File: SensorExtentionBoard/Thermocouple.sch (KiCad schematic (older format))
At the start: 13 parts

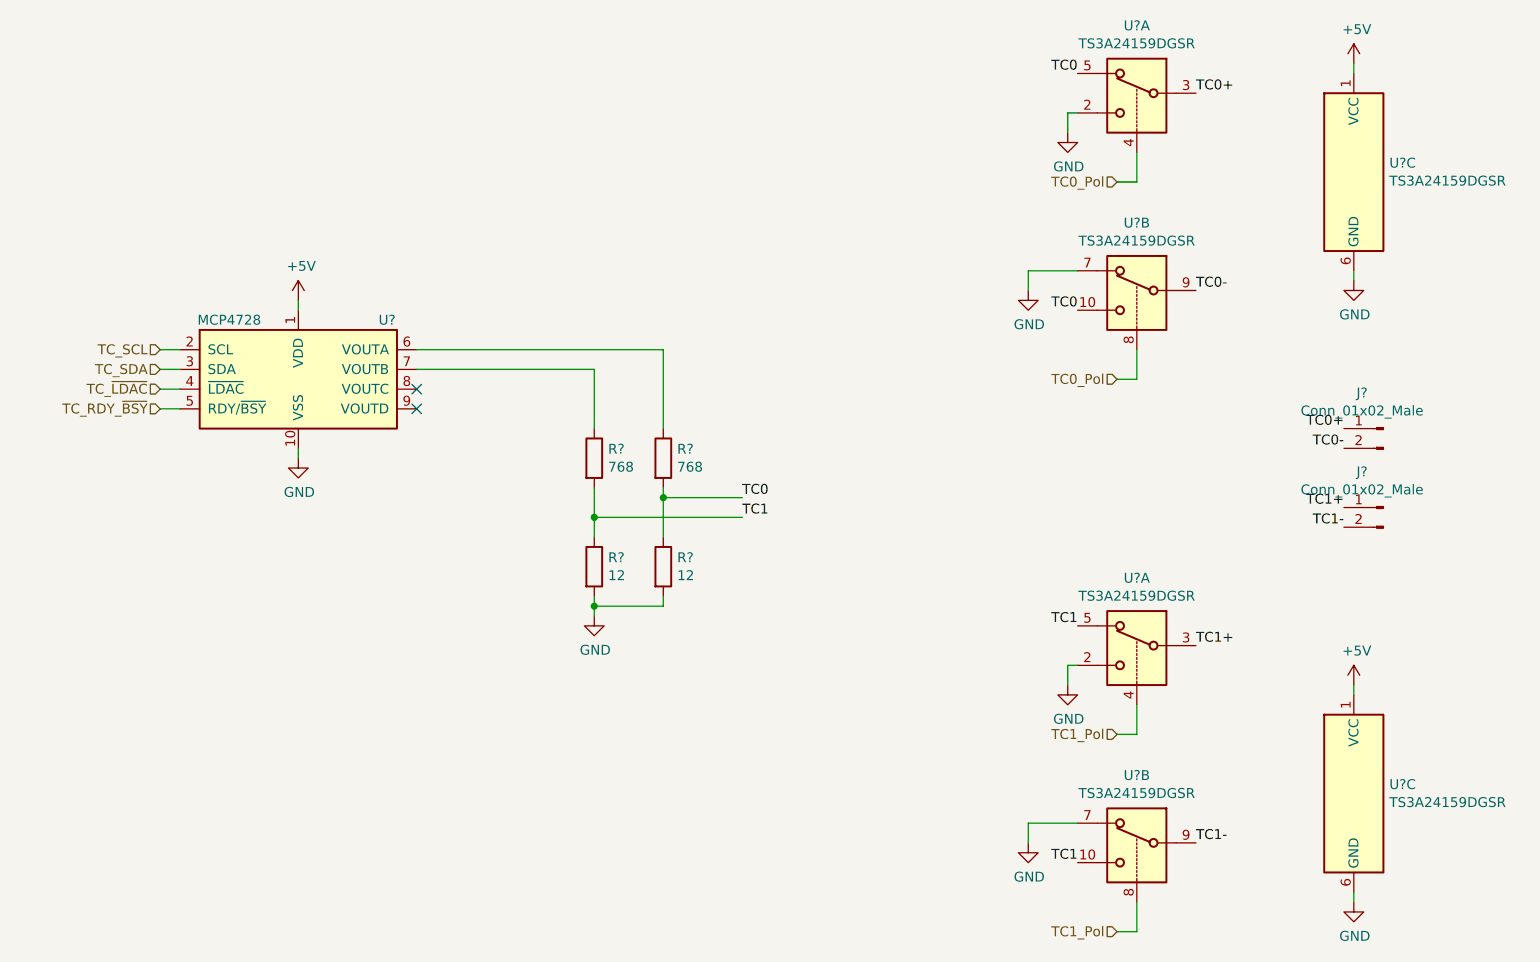
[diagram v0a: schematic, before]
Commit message: Added top level page and made various fixes in other pages of SEB test rig board
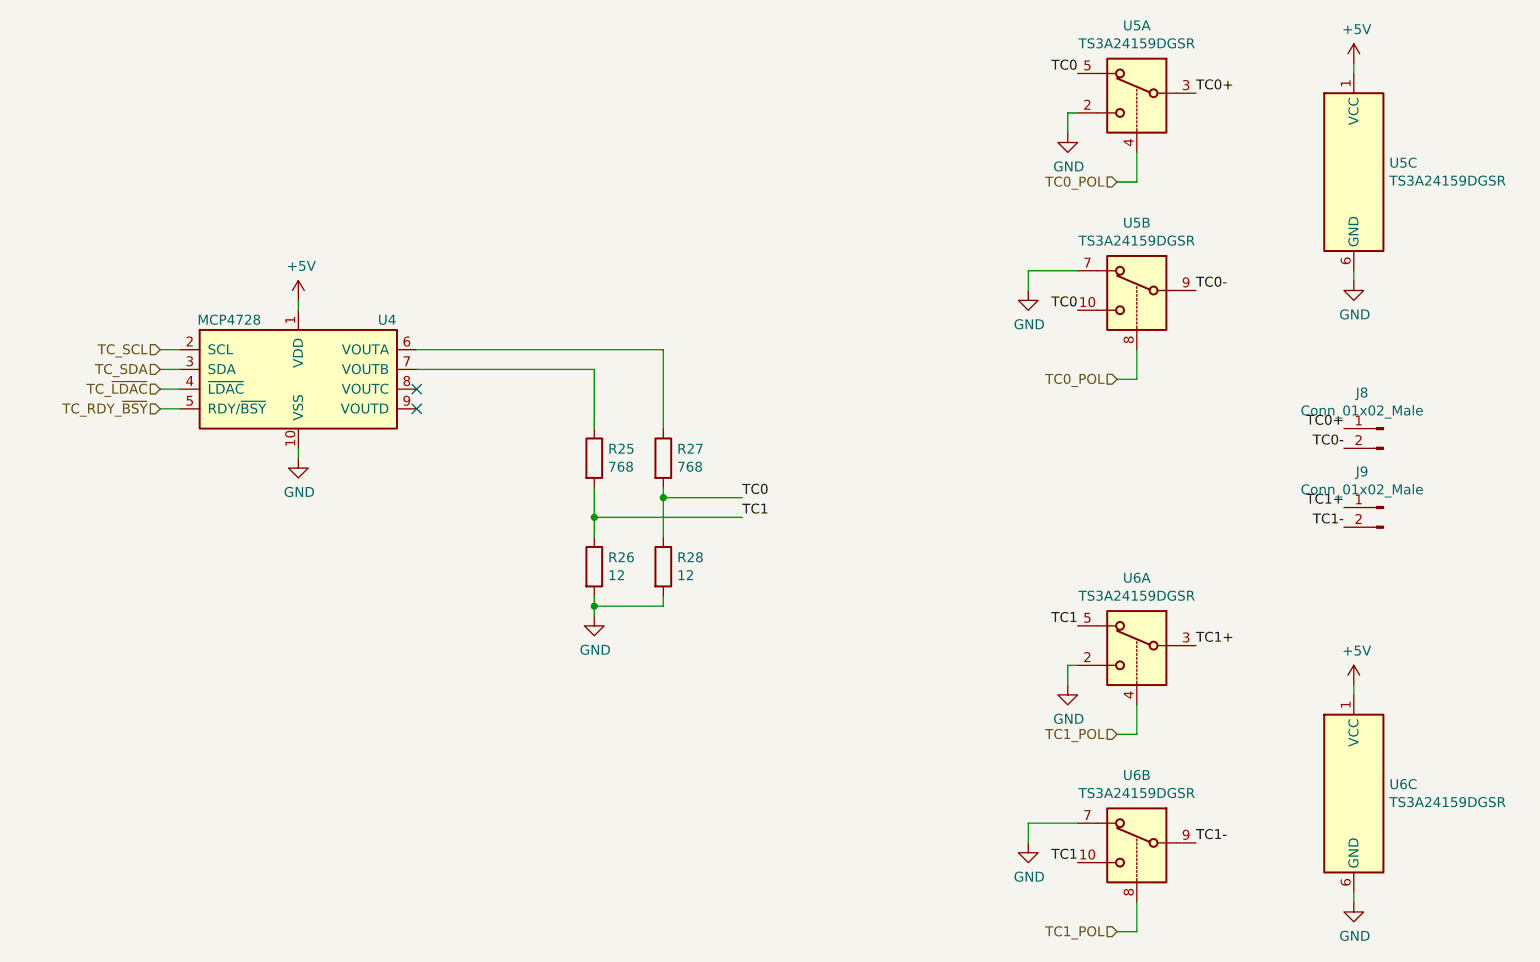
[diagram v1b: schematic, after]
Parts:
- R25, R26, R27, R28: renamed from R?; footprint (none) -> Resistor_SMD:R_1206_3216Metric_Pad1.42x1.75mm_HandSolder
- gave numbers to parts that had none: 5
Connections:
- net TC0_Pol renamed TC0_POL
- net TC1_Pol renamed TC1_POL
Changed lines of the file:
@@
 $EndDescr
 $Comp
-L Analog_DAC:MCP4728 U?
+L Analog_DAC:MCP4728 U4
 U 1 1 5E2FD865
 P 4000 2350
-F 0 "U?" H 4450 2600 50  0000 C CNN
+F 0 "U4" H 4450 2600 50  0000 C CNN
 F 1 "MCP4728" H 3650 2600 50  0000 C CNN
 F 2 "Package_SO:MSOP-10_3x3mm_P0.5mm" H 4000 1750 50  0001 C CNN
@@
 $EndComp
 $Comp
-L power:GND #PWR?
+L power:GND #PWR022
 U 1 1 5E2FE6B0
 P 4000 2800
-F 0 "#PWR?" H 4000 2550 50  0001 C CNN
+F 0 "#PWR022" H 4000 2550 50  0001 C CNN
 F 1 "GND" H 4005 2627 50  0000 C CNN
 F 2 "" H 4000 2800 50  0001 C CNN
@@
 	4000 2800 4000 2750
 $Comp
-L power:+5V #PWR?
+L power:+5V #PWR021
 U 1 1 5E2FE9D8
 P 4000 2000
-F 0 "#PWR?" H 4000 1850 50  0001 C CNN
+F 0 "#PWR021" H 4000 1850 50  0001 C CNN
 F 1 "+5V" H 4015 2173 50  0000 C CNN
 F 2 "" H 4000 2000 50  0001 C CNN
@@
 	3300 2450 3400 2450
 $Comp
-L Device:R R?
+L Device:R R27
 U 1 1 5E3006EF
 P 5850 2800
-F 0 "R?" H 5920 2846 50  0000 L CNN
+F 0 "R27" H 5920 2846 50  0000 L CNN
 F 1 "768" H 5920 2755 50  0000 L CNN
-F 2 "" V 5780 2800 50  0001 C CNN
+F 2 "Resistor_SMD:R_1206_3216Metric_Pad1.42x1.75mm_HandSolder" V 5780 2800 50  0001 C CNN
 F 3 "~" H 5850 2800 50  0001 C CNN
 	1    5850 2800
@@
 $EndComp
 $Comp
-L Device:R R?
+L Device:R R28
 U 1 1 5E300948
 P 5850 3350
-F 0 "R?" H 5920 3396 50  0000 L CNN
+F 0 "R28" H 5920 3396 50  0000 L CNN
 F 1 "12" H 5920 3305 50  0000 L CNN
-F 2 "" V 5780 3350 50  0001 C CNN
+F 2 "Resistor_SMD:R_1206_3216Metric_Pad1.42x1.75mm_HandSolder" V 5780 3350 50  0001 C CNN
 F 3 "~" H 5850 3350 50  0001 C CNN
 	1    5850 3350
@@
 $EndComp
 $Comp
-L Device:R R?
+L Device:R R25
 U 1 1 5E3082B4
 P 5500 2800
-F 0 "R?" H 5570 2846 50  0000 L CNN
+F 0 "R25" H 5570 2846 50  0000 L CNN
 F 1 "768" H 5570 2755 50  0000 L CNN
-F 2 "" V 5430 2800 50  0001 C CNN
+F 2 "Resistor_SMD:R_1206_3216Metric_Pad1.42x1.75mm_HandSolder" V 5430 2800 50  0001 C CNN
 F 3 "~" H 5500 2800 50  0001 C CNN
 	1    5500 2800
@@
 $EndComp
 $Comp
-L Device:R R?
+L Device:R R26
 U 1 1 5E3082BA
 P 5500 3350
-F 0 "R?" H 5570 3396 50  0000 L CNN
+F 0 "R26" H 5570 3396 50  0000 L CNN
 F 1 "12" H 5570 3305 50  0000 L CNN
-F 2 "" V 5430 3350 50  0001 C CNN
+F 2 "Resistor_SMD:R_1206_3216Metric_Pad1.42x1.75mm_HandSolder" V 5430 3350 50  0001 C CNN
 F 3 "~" H 5500 3350 50  0001 C CNN
 	1    5500 3350
@@
 	5500 3100 5500 3200
 $Comp
-L power:GND #PWR?
+L power:GND #PWR023
 U 1 1 5E3159B6
 P 5500 3600
-F 0 "#PWR?" H 5500 3350 50  0001 C CNN
+F 0 "#PWR023" H 5500 3350 50  0001 C CNN
 F 1 "GND" H 5505 3427 50  0000 C CNN
 F 2 "" H 5500 3600 50  0001 C CNN
@@
 NoConn ~ 4600 2450
 $Comp
-L Analog_Switch:TS3A24159DGSR U?
+L Analog_Switch:TS3A24159DGSR U5
 U 3 1 5E318CFB
 P 9350 1350
-F 0 "U?" H 9530 1396 50  0000 L CNN
+F 0 "U5" H 9530 1396 50  0000 L CNN
 F 1 "TS3A24159DGSR" H 9530 1305 50  0000 L CNN
 F 2 "Package_SO:TSSOP-10_3x3mm_P0.5mm" H 9350 1000 50  0001 C CNN
@@
 $EndComp
 $Comp
-L power:+5V #PWR?
+L power:+5V #PWR028
 U 1 1 5E33134D
 P 9350 800
-F 0 "#PWR?" H 9350 650 50  0001 C CNN
+F 0 "#PWR028" H 9350 650 50  0001 C CNN
 F 1 "+5V" H 9365 973 50  0000 C CNN
 F 2 "" H 9350 800 50  0001 C CNN
@@
 	9350 800  9350 850
 $Comp
-L power:GND #PWR?
+L power:GND #PWR029
 U 1 1 5E332A5C
 P 9350 1900
-F 0 "#PWR?" H 9350 1650 50  0001 C CNN
+F 0 "#PWR029" H 9350 1650 50  0001 C CNN
 F 1 "GND" H 9355 1727 50  0000 C CNN
 F 2 "" H 9350 1900 50  0001 C CNN
@@
 	8150 2400 8250 2400
 Text HLabel 8150 2400 0    50   Input ~ 0
-TC0_Pol
+TC0_POL
 Wire Wire Line
 	8250 1400 8250 1250
@@
 	8150 1400 8250 1400
 Text HLabel 8150 1400 0    50   Input ~ 0
-TC0_Pol
+TC0_POL
 Wire Wire Line
 	7900 1050 7950 1050
@@
 TC0
 $Comp
-L power:GND #PWR?
+L power:GND #PWR024
 U 1 1 5E324555
 P 7700 1950
-F 0 "#PWR?" H 7700 1700 50  0001 C CNN
+F 0 "#PWR024" H 7700 1700 50  0001 C CNN
 F 1 "GND" H 7705 1777 50  0000 C CNN
 F 2 "" H 7700 1950 50  0001 C CNN
@@
 $EndComp
 $Comp
-L power:GND #PWR?
+L power:GND #PWR026
 U 1 1 5E324066
 P 7900 1150
-F 0 "#PWR?" H 7900 900 50  0001 C CNN
+F 0 "#PWR026" H 7900 900 50  0001 C CNN
 F 1 "GND" H 7905 977 50  0000 C CNN
 F 2 "" H 7900 1150 50  0001 C CNN
@@
 TC0+
 $Comp
-L Analog_Switch:TS3A24159DGSR U?
+L Analog_Switch:TS3A24159DGSR U5
 U 2 1 5E317F40
 P 8250 1850
-F 0 "U?" H 8250 2092 50  0000 C CNN
+F 0 "U5" H 8250 2092 50  0000 C CNN
 F 1 "TS3A24159DGSR" H 8250 2001 50  0000 C CNN
 F 2 "Package_SO:TSSOP-10_3x3mm_P0.5mm" H 8250 1500 50  0001 C CNN
@@
 $EndComp
 $Comp
-L Analog_Switch:TS3A24159DGSR U?
+L Analog_Switch:TS3A24159DGSR U5
 U 1 1 5E31745F
 P 8250 850
-F 0 "U?" H 8250 1092 50  0000 C CNN
+F 0 "U5" H 8250 1092 50  0000 C CNN
 F 1 "TS3A24159DGSR" H 8250 1001 50  0000 C CNN
 F 2 "Package_SO:TSSOP-10_3x3mm_P0.5mm" H 8250 500 50  0001 C CNN
@@
 $EndComp
 $Comp
-L Analog_Switch:TS3A24159DGSR U?
+L Analog_Switch:TS3A24159DGSR U6
 U 3 1 5E35C1F5
 P 9350 4500
-F 0 "U?" H 9530 4546 50  0000 L CNN
+F 0 "U6" H 9530 4546 50  0000 L CNN
 F 1 "TS3A24159DGSR" H 9530 4455 50  0000 L CNN
 F 2 "Package_SO:TSSOP-10_3x3mm_P0.5mm" H 9350 4150 50  0001 C CNN
@@
 $EndComp
 $Comp
-L power:+5V #PWR?
+L power:+5V #PWR030
 U 1 1 5E35C1FB
 P 9350 3950
-F 0 "#PWR?" H 9350 3800 50  0001 C CNN
+F 0 "#PWR030" H 9350 3800 50  0001 C CNN
 F 1 "+5V" H 9365 4123 50  0000 C CNN
 F 2 "" H 9350 3950 50  0001 C CNN
@@
 	9350 3950 9350 4000
 $Comp
-L power:GND #PWR?
+L power:GND #PWR031
 U 1 1 5E35C202
 P 9350 5050
-F 0 "#PWR?" H 9350 4800 50  0001 C CNN
+F 0 "#PWR031" H 9350 4800 50  0001 C CNN
 F 1 "GND" H 9355 4877 50  0000 C CNN
 F 2 "" H 9350 5050 50  0001 C CNN
@@
 	8150 5200 8250 5200
 Text HLabel 8150 5200 0    50   Input ~ 0
-TC1_Pol
+TC1_POL
 Wire Wire Line
 	8250 4200 8250 4050
@@
 	8150 4200 8250 4200
 Text HLabel 8150 4200 0    50   Input ~ 0
-TC1_Pol
+TC1_POL
 Wire Wire Line
 	7900 3850 7950 3850
@@
 TC1
 $Comp
-L power:GND #PWR?
+L power:GND #PWR025
 U 1 1 5E35C215
 P 7700 4750
-F 0 "#PWR?" H 7700 4500 50  0001 C CNN
+F 0 "#PWR025" H 7700 4500 50  0001 C CNN
 F 1 "GND" H 7705 4577 50  0000 C CNN
 F 2 "" H 7700 4750 50  0001 C CNN
@@
 $EndComp
 $Comp
-L power:GND #PWR?
+L power:GND #PWR027
 U 1 1 5E35C21B
 P 7900 3950
-F 0 "#PWR?" H 7900 3700 50  0001 C CNN
+F 0 "#PWR027" H 7900 3700 50  0001 C CNN
 F 1 "GND" H 7905 3777 50  0000 C CNN
 F 2 "" H 7900 3950 50  0001 C CNN
@@
 TC1+
 $Comp
-L Analog_Switch:TS3A24159DGSR U?
+L Analog_Switch:TS3A24159DGSR U6
 U 2 1 5E35C223
 P 8250 4650
-F 0 "U?" H 8250 4892 50  0000 C CNN
+F 0 "U6" H 8250 4892 50  0000 C CNN
 F 1 "TS3A24159DGSR" H 8250 4801 50  0000 C CNN
 F 2 "Package_SO:TSSOP-10_3x3mm_P0.5mm" H 8250 4300 50  0001 C CNN
@@
 $EndComp
 $Comp
-L Analog_Switch:TS3A24159DGSR U?
+L Analog_Switch:TS3A24159DGSR U6
 U 1 1 5E35C229
 P 8250 3650
-F 0 "U?" H 8250 3892 50  0000 C CNN
+F 0 "U6" H 8250 3892 50  0000 C CNN
 F 1 "TS3A24159DGSR" H 8250 3801 50  0000 C CNN
 F 2 "Package_SO:TSSOP-10_3x3mm_P0.5mm" H 8250 3300 50  0001 C CNN
@@
 $EndComp
 $Comp
-L Connector:Conn_01x02_Male J?
+L Connector:Conn_01x02_Male J8
 U 1 1 5E388A81
 P 9500 2650
-F 0 "J?" H 9608 2831 50  0000 C CNN
+F 0 "J8" H 9608 2831 50  0000 C CNN
 F 1 "Conn_01x02_Male" H 9608 2740 50  0000 C CNN
 F 2 "" H 9500 2650 50  0001 C CNN
@@
 $EndComp
 $Comp
-L Connector:Conn_01x02_Male J?
+L Connector:Conn_01x02_Male J9
 U 1 1 5E391340
 P 9500 3050
-F 0 "J?" H 9608 3231 50  0000 C CNN
+F 0 "J9" H 9608 3231 50  0000 C CNN
 F 1 "Conn_01x02_Male" H 9608 3140 50  0000 C CNN
 F 2 "" H 9500 3050 50  0001 C CNN

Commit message: Moved some stuff and added footprints to components
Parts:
- J8, J9: footprint (none) -> Connector_Molex:Molex_MicroClasp_55932-0210_1x02_P2.00mm_Vertical
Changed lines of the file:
@@
 F 0 "J8" H 9608 2831 50  0000 C CNN
 F 1 "Conn_01x02_Male" H 9608 2740 50  0000 C CNN
-F 2 "" H 9500 2650 50  0001 C CNN
+F 2 "Connector_Molex:Molex_MicroClasp_55932-0210_1x02_P2.00mm_Vertical" H 9500 2650 50  0001 C CNN
 F 3 "~" H 9500 2650 50  0001 C CNN
 	1    9500 2650
@@
 F 0 "J9" H 9608 3231 50  0000 C CNN
 F 1 "Conn_01x02_Male" H 9608 3140 50  0000 C CNN
-F 2 "" H 9500 3050 50  0001 C CNN
+F 2 "Connector_Molex:Molex_MicroClasp_55932-0210_1x02_P2.00mm_Vertical" H 9500 3050 50  0001 C CNN
 F 3 "~" H 9500 3050 50  0001 C CNN
 	1    9500 3050
